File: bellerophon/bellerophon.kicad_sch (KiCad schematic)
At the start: 34 parts, among them Q1 ST3413A, Q2 IRLL014NPBF, Q3 IRLL014NPBF, U1 HT7350-A, U2 Adafruit_ICM20948, U3 MPL3115A2, U4 Teensy4.0, U5 XTSD

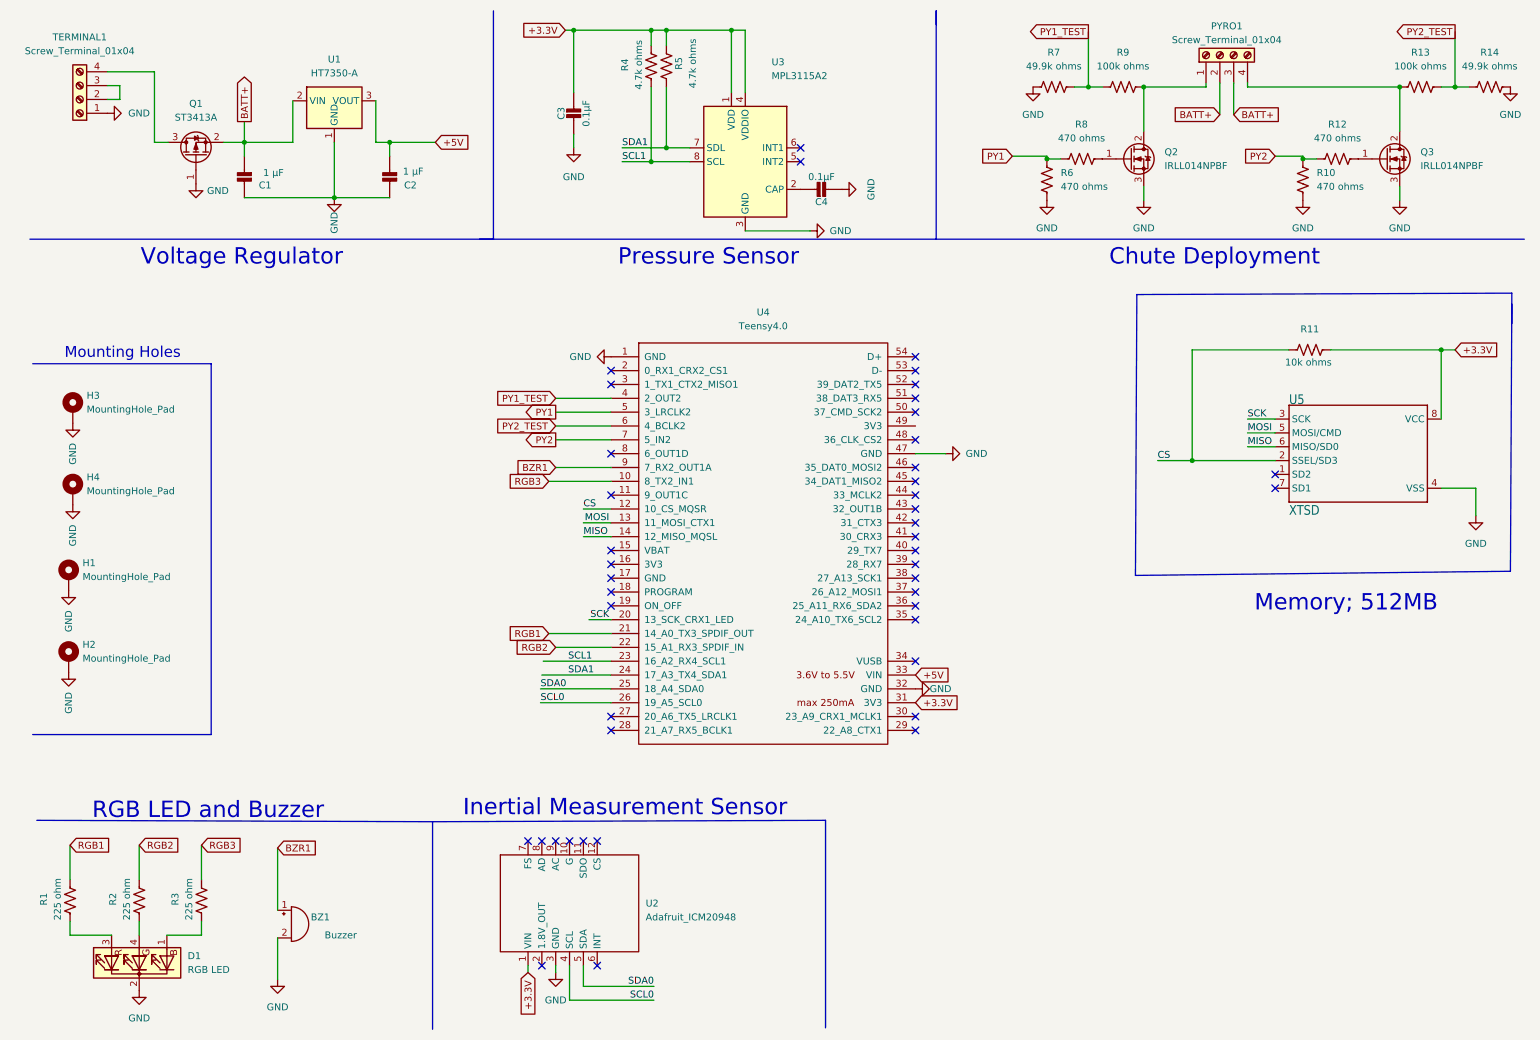
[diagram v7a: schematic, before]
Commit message: Replace ICM breakout board schematic with SMT BNO055 circuit
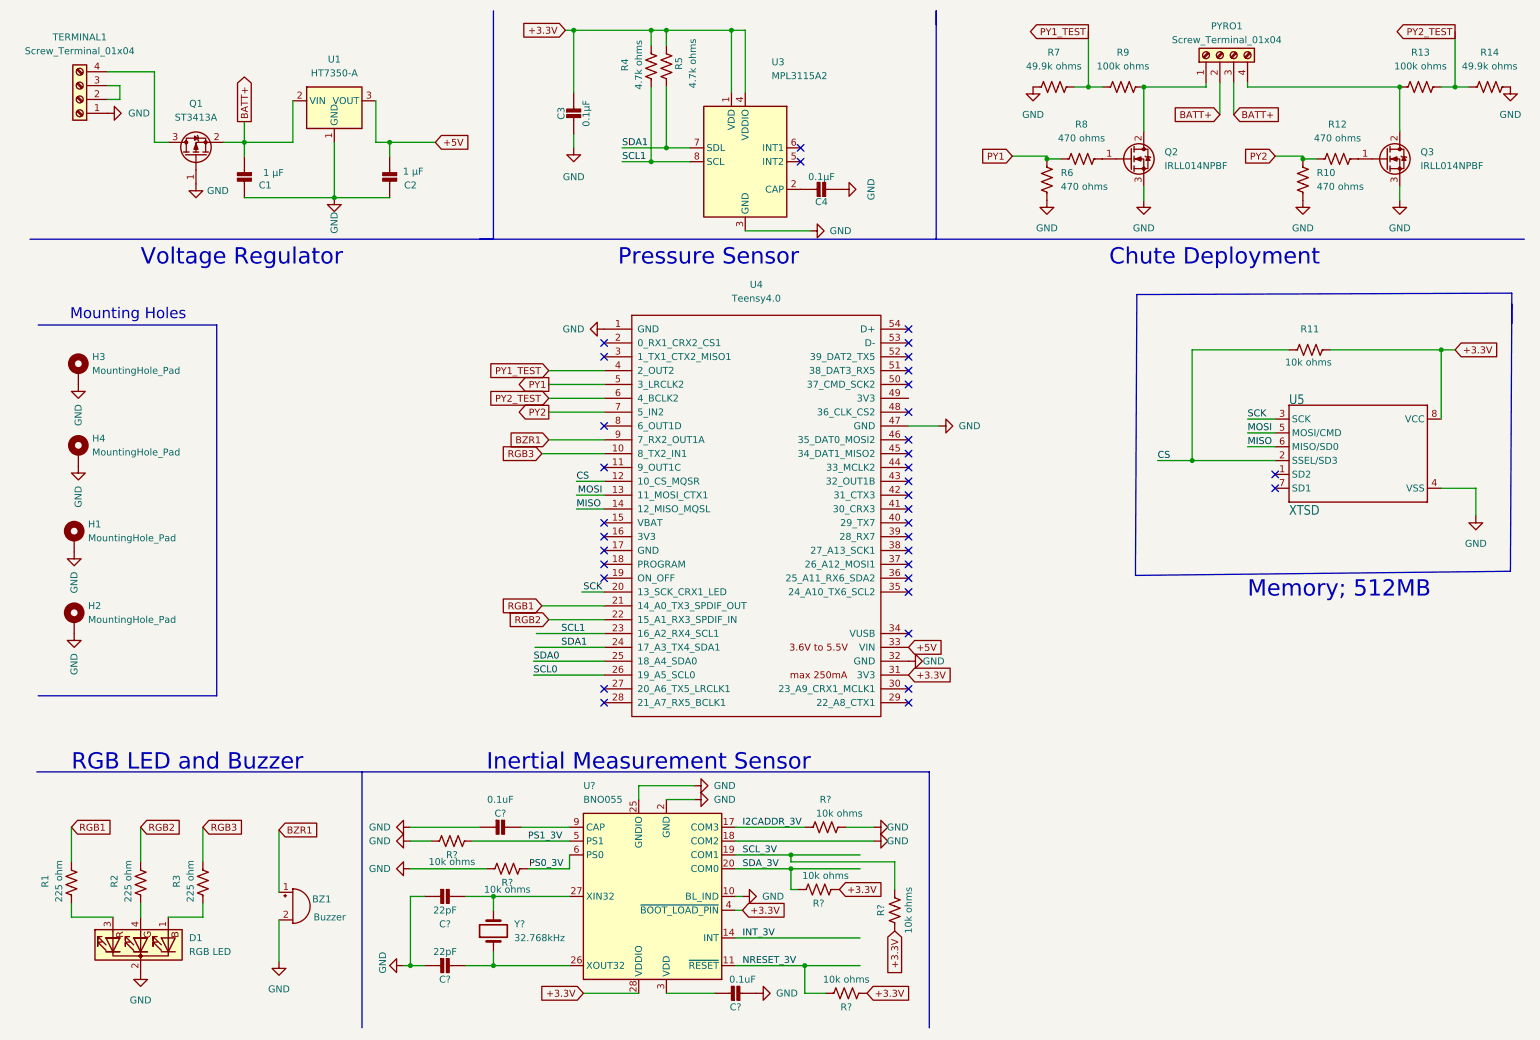
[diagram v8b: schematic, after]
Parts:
- removed U2: Adafruit_ICM20948, Adafruit:ICM20946-B25.4x17.78mm-2X06_ROUND-P2.54mm, symbol Adafruit:Adafruit_ICM20948
- added C? (x2): 0.1uF, Capacitor_SMD:C_0805_2012Metric_Pad1.18x1.45mm_HandSolder, symbol MPL3115A2_v0.2-eagle-import:CAP_CERAMIC0805-NOOUTLINE
- added C? (x2): 22pF, Capacitor_SMD:C_0805_2012Metric_Pad1.18x1.45mm_HandSolder, symbol MPL3115A2_v0.2-eagle-import:CAP_CERAMIC0805-NOOUTLINE
- added R? (x6): 10k ohms, Resistor_SMD:R_1206_3216Metric_Pad1.30x1.75mm_HandSolder, symbol Device:R_US
- added U?: BNO055, Package_LGA:LGA-28_5.2x3.8mm_P0.5mm, symbol Sensor_Motion:BNO055
- added Y?: 32.768kHz, symbol Device:Crystal
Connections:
- net +3.3V: now also R?.2, R?.2, R?.2, U?.28 (VDDIO), U?.4 (~{BOOT_LOAD_PIN})
- net GND: now also C?.2, C?.2, C?.2, C?.2, R?.1, R?.2, R?.2, U?.10 (BL_IND), U?.15 (GNDIO), U?.16 (GNDIO), U?.18 (COM2), U?.2 (GND), U?.25 (GNDIO)
- new net: R?.1, U?.6 (PS0)
- new net: C?.1, U?.3 (VDD)
- new net: C?.1, U?.26 (XOUT32), Y?.1
- new net: C?.1, U?.27 (XIN32), Y?.2
- new net: C?.1, U?.9 (CAP)
- new net I2CADDR_3V: R?.2, U?.17 (COM3)
- new net INT_3V: U?.14 (INT)
- new net NRESET_3V: R?.1, U?.11 (~{RESET})
- new net PS1_3V: R?.1, U?.5 (PS1)
- new net SCL_3V: R?.1, U?.19 (COM1)
- new net SDA_3V: R?.1, U?.20 (COM0)
- no-connect marks 44 -> 36
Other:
- moved on the sheet: BZ1, D1, H1, H2, H3, H4, R1, R2, R3, U4
